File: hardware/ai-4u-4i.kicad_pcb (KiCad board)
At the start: 4 copper layers, 100 x 85 mm, 207 parts, among them J101 TNG-Power-TOP, J102 TNG-Power-BTM, J103 TNG-Data-TOP, J104 TNG-Data-BTM, P102 Debug, P103 PE, P201 INPUT0, P202 INPUT1, P203 INPUT2, P204 INPUT3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

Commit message: fix values
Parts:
- C113, C114: value TBD/47pF -> 47pF

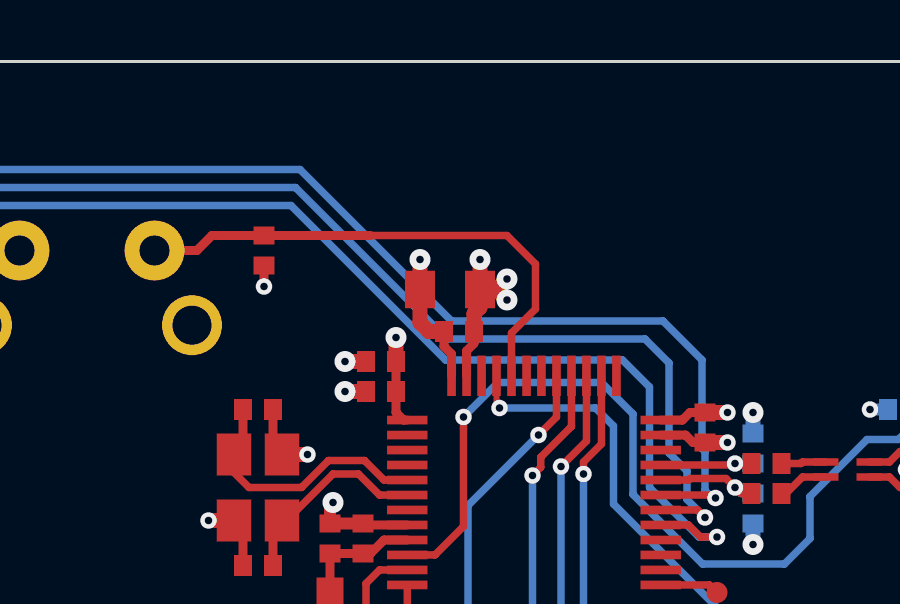
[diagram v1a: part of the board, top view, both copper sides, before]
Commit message: fix footprint
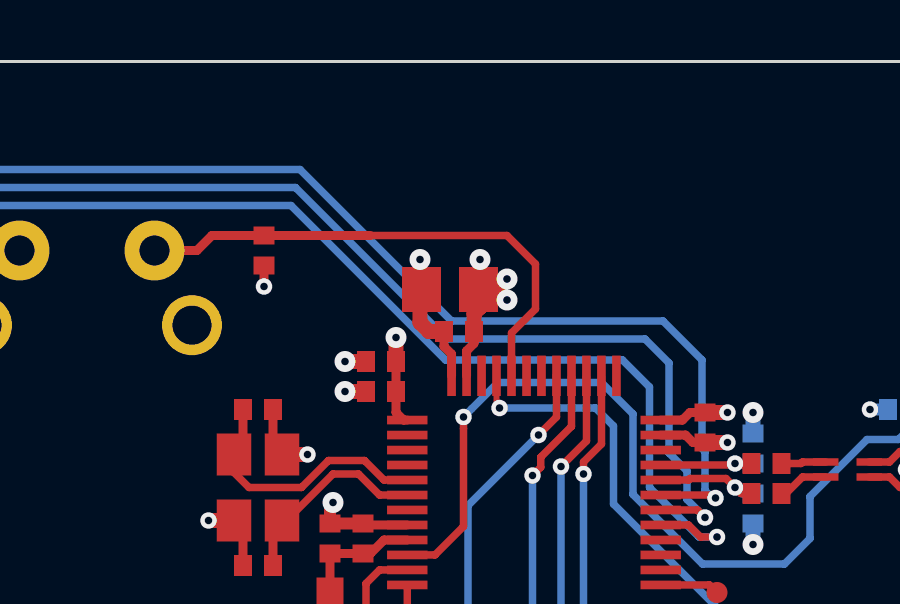
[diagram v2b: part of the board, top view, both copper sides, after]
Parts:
- C110: footprint C0805 -> kicad-libraries:C0805E

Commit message: fix values
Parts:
- C111: value 100µF -> 100uF
- C118: value 10µF/50V -> 10uF/50V
- C121, C125, C126: value 10µF/35V -> 10uF/35V
- C122, C123, C124, C234: value 100µF/35V -> 100uF/35V
- C230, C231: value 10µF -> 10uF
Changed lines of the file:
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@@
       (effects (font (size 0.3 0.3) (thickness 0.075)))
     )
-    (fp_text value 10µF (at 0 -0.65) (layer F.Fab)
+    (fp_text value 10uF (at 0 -0.65) (layer F.Fab)
       (effects (font (size 0.3 0.3) (thickness 0.075)))
     )
@@
       (effects (font (size 0.3 0.3) (thickness 0.075)) (justify mirror))
     )
-    (fp_text value 10µF (at 0 0.65 270) (layer B.Fab)
+    (fp_text value 10uF (at 0 0.65 270) (layer B.Fab)
       (effects (font (size 0.3 0.3) (thickness 0.075)) (justify mirror))
     )
@@
       (effects (font (size 0.3 0.3) (thickness 0.075)))
     )
-    (fp_text value 10µF/50V (at 0 -0.65 -180) (layer F.Fab)
+    (fp_text value 10uF/50V (at 0 -0.65 -180) (layer F.Fab)
       (effects (font (size 0.3 0.3) (thickness 0.075)))
     )
@@
       (effects (font (size 0.3 0.3) (thickness 0.075)) (justify mirror))
     )
-    (fp_text value 10µF/35V (at 0 0.65 90) (layer B.Fab)
+    (fp_text value 10uF/35V (at 0 0.65 90) (layer B.Fab)
       (effects (font (size 0.3 0.3) (thickness 0.075)) (justify mirror))
     )
@@
       (effects (font (size 0.3 0.3) (thickness 0.075)))
     )
-    (fp_text value 10µF/35V (at 0 -0.65) (layer F.Fab)
+    (fp_text value 10uF/35V (at 0 -0.65) (layer F.Fab)
       (effects (font (size 0.3 0.3) (thickness 0.075)))
     )
@@
       (effects (font (size 0.3 0.3) (thickness 0.075)))
     )
-    (fp_text value 10µF/35V (at 0 -0.65) (layer F.Fab)
+    (fp_text value 10uF/35V (at 0 -0.65) (layer F.Fab)
       (effects (font (size 0.3 0.3) (thickness 0.075)))
     )
@@
       (effects (font (size 0.59944 0.59944) (thickness 0.12446)))
     )
-    (fp_text value 100µF (at 0.95 -0.375) (layer F.Fab)
+    (fp_text value 100uF (at 0.95 -0.375) (layer F.Fab)
       (effects (font (size 0.59944 0.59944) (thickness 0.12446)))
     )
@@
       (effects (font (size 0.59944 0.59944) (thickness 0.12446)))
     )
-    (fp_text value 100µF/35V (at 0.95 -0.375 90) (layer F.Fab)
+    (fp_text value 100uF/35V (at 0.95 -0.375 90) (layer F.Fab)
       (effects (font (size 0.59944 0.59944) (thickness 0.12446)))
     )
@@
       (effects (font (size 0.59944 0.59944) (thickness 0.12446)))
     )
-    (fp_text value 100µF/35V (at 0.95 -0.375) (layer F.Fab)
+    (fp_text value 100uF/35V (at 0.95 -0.375) (layer F.Fab)
       (effects (font (size 0.59944 0.59944) (thickness 0.12446)))
     )
@@
       (effects (font (size 0.59944 0.59944) (thickness 0.12446)))
     )
-    (fp_text value 100µF/35V (at 0.95 -0.375 90) (layer F.Fab)
+    (fp_text value 100uF/35V (at 0.95 -0.375 90) (layer F.Fab)
       (effects (font (size 0.59944 0.59944) (thickness 0.12446)))
     )
@@
       (effects (font (size 0.59944 0.59944) (thickness 0.12446)))
     )
-    (fp_text value 100µF/35V (at 0.95 -0.375) (layer F.Fab)
+    (fp_text value 100uF/35V (at 0.95 -0.375) (layer F.Fab)
       (effects (font (size 0.59944 0.59944) (thickness 0.12446)))
     )

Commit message: fix footprints
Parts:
- R209, R210, R211, R212, R213, R214, R215, R216: footprint kicad-libraries:R0805 -> kicad-libraries:R0805E

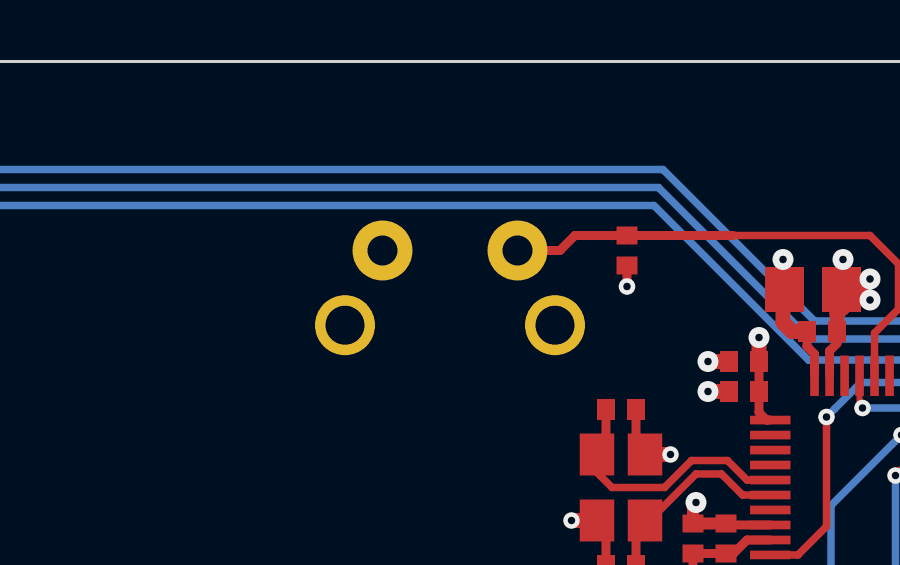
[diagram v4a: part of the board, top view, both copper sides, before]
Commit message: all footprints updated
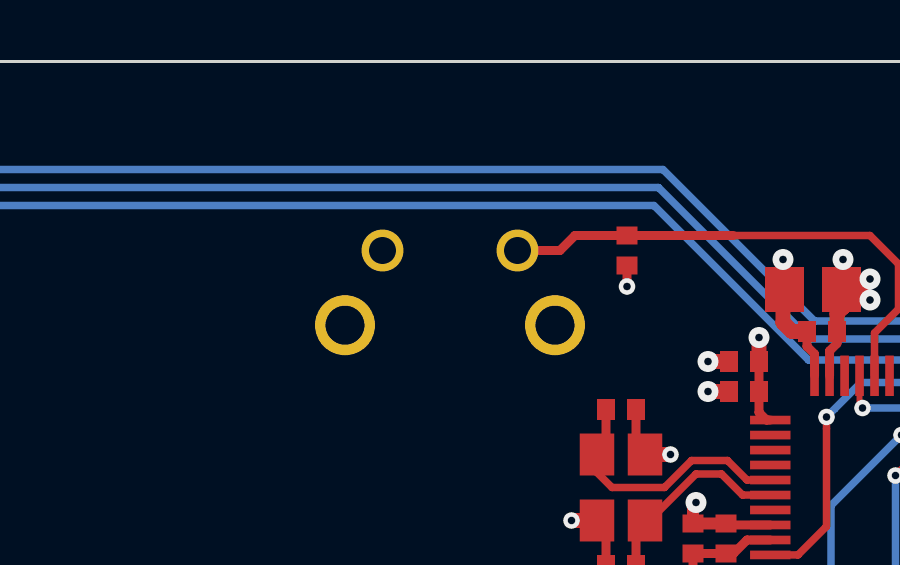
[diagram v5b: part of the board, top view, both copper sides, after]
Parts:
- C101, C102, C103, C104, C105, C106, C107, C108, C109, C112, C113, C114, C116, C117: footprint C0402F -> kicad-libraries:C0402F
- C115: footprint C0603F -> kicad-libraries:C0603F
- C118, C119, C120, C121, C125, C126, C127, C128: footprint C1206 -> kicad-libraries:C1206
- D203, D204, D205, D206, D207, D208, D209, D210: footprint LED-LP -> kicad-libraries:LED-LP
- J101, J103: footprint TNG-40-TOP -> kicad-libraries:TNG-40-TOP
- J102, J104: footprint TNG-40-BTM -> kicad-libraries:TNG-40-BTM
- L101, L102, L103, L104: footprint R0603F -> kicad-libraries:R0603F
- L105: footprint WE-CNSW-0603 -> kicad-libraries:WE-CNSW-0603
- LED101: footprint LED-RGB-LP -> kicad-libraries:LED-RGB-LP
- P201, P202, P203, P204: footprint OQ_4P -> kicad-libraries:OQ_4P
- R101, R102, R103, R104, R105, R106, R107, R108: footprint R0402F -> kicad-libraries:R0402F
- U103: footprint SOT563-SPEC -> kicad-libraries:SOT563-SPEC

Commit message: fix 3d stuff
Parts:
- C119, C120: value 1nF 2kV -> 0
- C201, C202, C203, C204, C205, C206, C207, C208: value 27nF -> 22nF
- C209, C210, C211, C212, C213, C214, C215, C216: value 2700pF -> 2200pF
- U104: value TEL10 -> DNP
